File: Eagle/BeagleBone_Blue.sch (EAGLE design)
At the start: 146 parts, among them M1 JST_ZH_2, M2 JST_ZH_2, M3 JST_ZH_2, M4 JST_ZH_2, Q3 MOSFET-N, U1 OSD3358

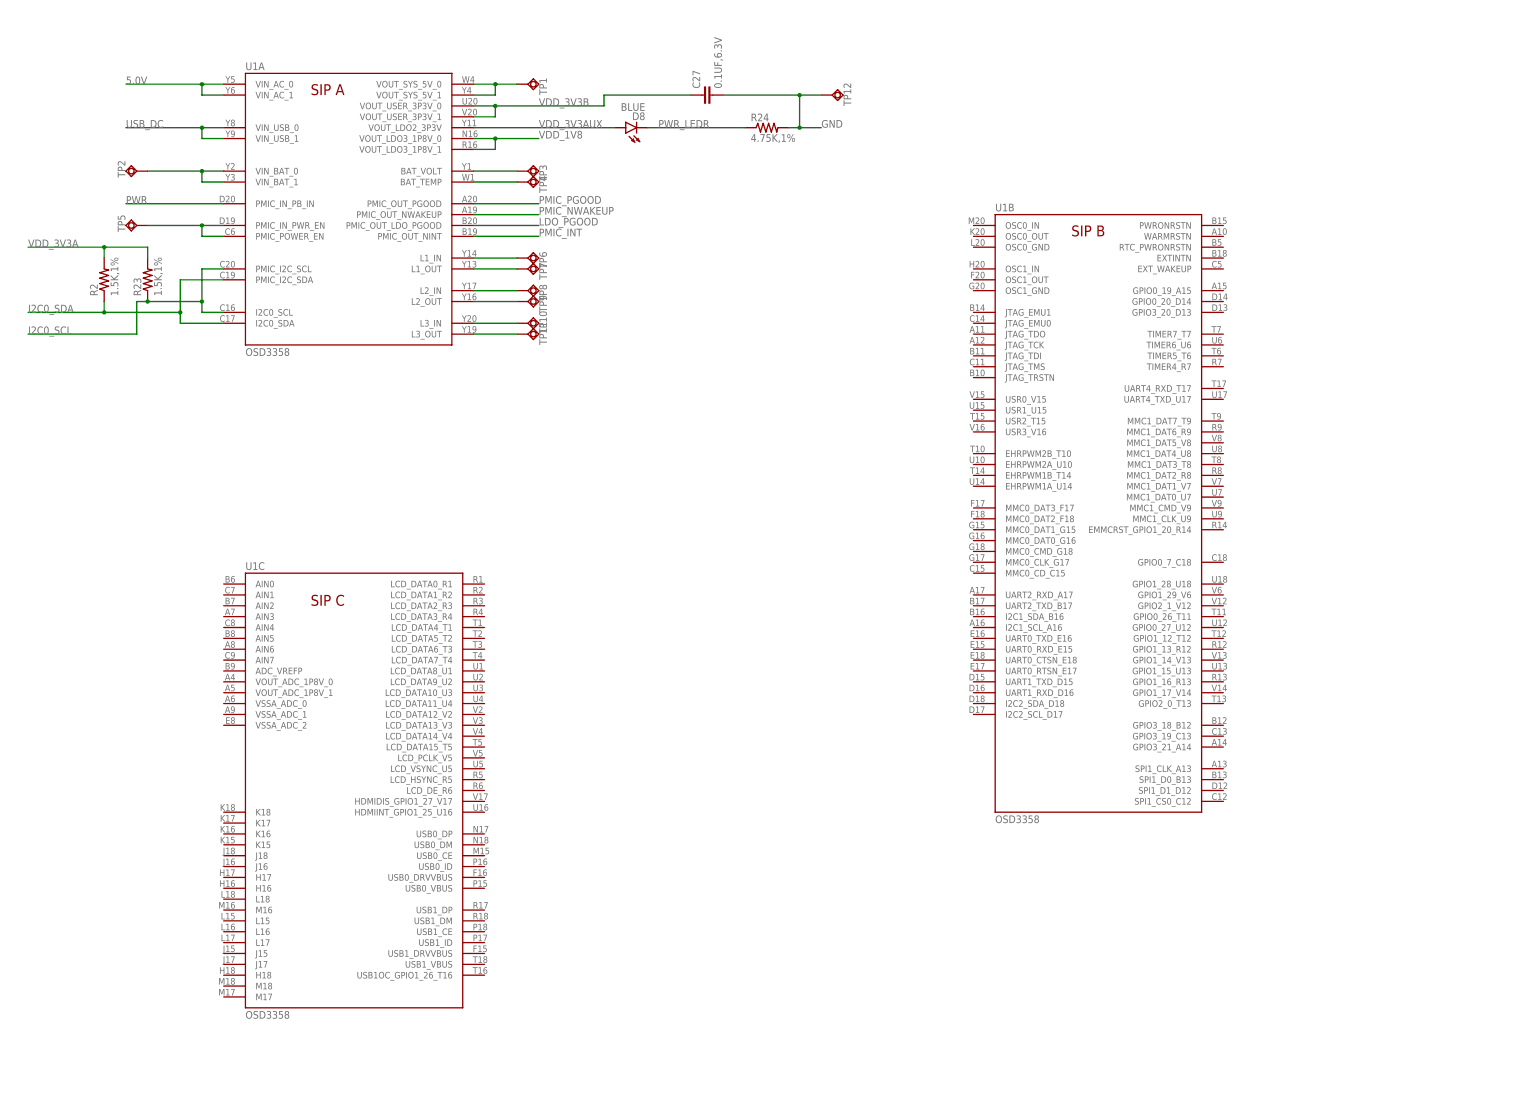
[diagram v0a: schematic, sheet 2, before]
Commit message: Add EEPROM
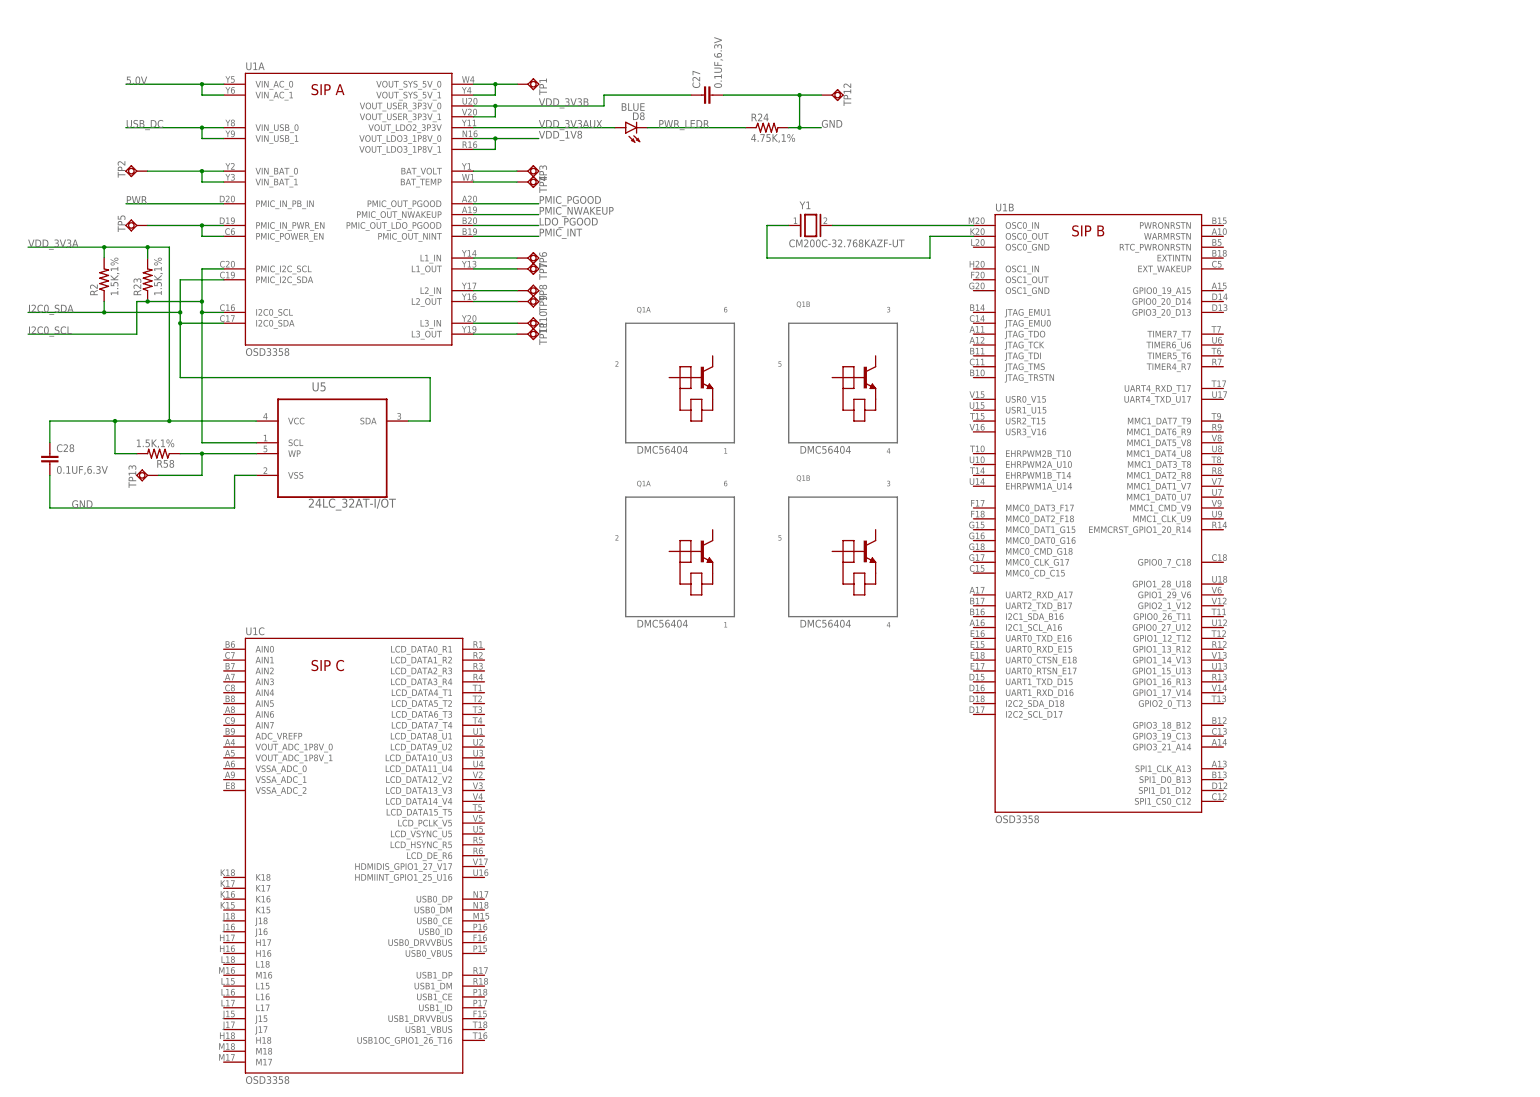
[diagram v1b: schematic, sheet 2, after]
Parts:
- added C28: 0.1UF,6.3V, Strawson_Eagle_Lib:CAP0402-CAP
- added R58: 1.5K,1%, Strawson_Eagle_Lib:RESISTOR0402-RES
- added TP13: TPSQB1,27, testpad:TPSQB1,27
- added U2: CM200C-32.768KAZF-UT, CM200C-32.768KAZF-UT:CM200C-32.768KAZF-UT
- added U3, U4: DMC564040R, DMC564040R:DMC564040R
- added U5: 24LC_32AT-I/OT, Microchip-24LCxxx:24LC_32AT-I/OT
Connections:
- new net N$26: U1B.OSC0_IN, U2.2
- new net N$27: U1B.OSC0_OUT, U2.1
- new net N$28: R58.1, TP13.TP, U5.WP
- net GND: now also C28.2, U5.VSS
- net I2C0_SDA: now also U5.SDA
- net VDD_3V3A: now also C28.1, R58.2, U5.VCC
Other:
- moved on the sheet: U1C
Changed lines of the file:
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@@
 <part name="TP12" library="testpad" deviceset="TPSQ" device="B1,27"/>
 <part name="C27" library="Strawson_Eagle_Lib" deviceset="CAP" device="0402-CAP" value="0.1UF,6.3V"/>
+<part name="U2" library="CM200C-32.768KAZF-UT" deviceset="CM200C-32.768KAZF-UT" device=""/>
+<part name="U3" library="DMC564040R" deviceset="DMC564040R" device=""/>
+<part name="U4" library="DMC564040R" deviceset="DMC564040R" device=""/>
+<part name="U5" library="Microchip-24LCxxx" deviceset="24LC_" device="" technology="32AT-I/OT"/>
+<part name="R58" library="Strawson_Eagle_Lib" deviceset="RESISTOR" device="0402-RES" value="1.5K,1%"/>
+<part name="TP13" library="testpad" deviceset="TPSQ" device="B1,27"/>
+<part name="C28" library="Strawson_Eagle_Lib" deviceset="CAP" device="0402-CAP" value="0.1UF,6.3V"/>
 </parts>
 <sheets>
@@
 <instance part="U1" gate="B" x="246.38" y="78.74"/>
 <instance part="U1" gate="A" x="71.12" y="187.96"/>
-<instance part="U1" gate="C" x="71.12" y="33.02"/>
+<instance part="U1" gate="C" x="71.12" y="17.78"/>
 <instance part="TP1" gate="G$1" x="137.16" y="248.92" rot="R90"/>
 <instance part="TP2" gate="G$1" x="45.72" y="228.6" rot="R270"/>
@@
 <instance part="TP12" gate="G$1" x="208.28" y="246.38" rot="R90"/>
 <instance part="C27" gate="G$1" x="180.34" y="246.38" rot="R90"/>
+<instance part="U2" gate="G$1" x="251.46" y="203.2"/>
+<instance part="U3" gate="G$1" x="195.58" y="175.26"/>
+<instance part="U4" gate="G$1" x="195.58" y="134.62"/>
+<instance part="U5" gate="A" x="73.66" y="170.18"/>
+<instance part="R58" gate="G$1" x="50.8" y="162.56" rot="R180"/>
+<instance part="TP13" gate="G$1" x="48.26" y="157.48" rot="R270"/>
+<instance part="C28" gate="G$1" x="25.4" y="160.02"/>
 </instances>
 <busses>
@@
 <wire x1="45.72" y1="190.5" x2="20.32" y2="190.5" width="0.1524" layer="91"/>
 <label x="20.32" y="190.5" size="1.778" layer="95"/>
+<wire x1="60.96" y1="195.58" x2="60.96" y2="165.1" width="0.1524" layer="91"/>
+<junction x="60.96" y="195.58"/>
+<wire x1="60.96" y1="165.1" x2="73.66" y2="165.1" width="0.1524" layer="91"/>
 </segment>
 </net>
@@
 <junction x="38.1" y="195.58"/>
 <label x="20.32" y="195.58" size="1.778" layer="95"/>
+<wire x1="55.88" y1="193.04" x2="55.88" y2="180.34" width="0.1524" layer="91"/>
+<junction x="55.88" y="193.04"/>
+<wire x1="55.88" y1="180.34" x2="114.3" y2="180.34" width="0.1524" layer="91"/>
+<wire x1="114.3" y1="180.34" x2="114.3" y2="170.18" width="0.1524" layer="91"/>
+<wire x1="114.3" y1="170.18" x2="109.22" y2="170.18" width="0.1524" layer="91"/>
+<pinref part="U5" gate="A" pin="SDA"/>
 </segment>
 </net>
@@
 <junction x="38.1" y="210.82"/>
 <label x="20.32" y="210.82" size="1.778" layer="95"/>
+<wire x1="48.26" y1="210.82" x2="53.34" y2="210.82" width="0.1524" layer="91"/>
+<junction x="48.26" y="210.82"/>
+<wire x1="53.34" y1="210.82" x2="53.34" y2="170.18" width="0.1524" layer="91"/>
+<pinref part="U5" gate="A" pin="VCC"/>
+<wire x1="53.34" y1="170.18" x2="73.66" y2="170.18" width="0.1524" layer="91"/>
+<wire x1="53.34" y1="170.18" x2="40.64" y2="170.18" width="0.1524" layer="91"/>
+<junction x="53.34" y="170.18"/>
+<wire x1="40.64" y1="170.18" x2="40.64" y2="162.56" width="0.1524" layer="91"/>
+<pinref part="R58" gate="G$1" pin="2"/>
+<wire x1="40.64" y1="162.56" x2="45.72" y2="162.56" width="0.1524" layer="91"/>
+<pinref part="C28" gate="G$1" pin="1"/>
+<wire x1="40.64" y1="170.18" x2="25.4" y2="170.18" width="0.1524" layer="91"/>
+<wire x1="25.4" y1="170.18" x2="25.4" y2="165.1" width="0.1524" layer="91"/>
+<junction x="40.64" y="170.18"/>
 </segment>
 </net>
@@
 <junction x="200.66" y="238.76"/>
 </segment>
+<segment>
+<pinref part="U5" gate="A" pin="VSS"/>
+<wire x1="73.66" y1="157.48" x2="68.58" y2="157.48" width="0.1524" layer="91"/>
+<wire x1="68.58" y1="157.48" x2="68.58" y2="149.86" width="0.1524" layer="91"/>
+<wire x1="68.58" y1="149.86" x2="25.4" y2="149.86" width="0.1524" layer="91"/>
+<pinref part="C28" gate="G$1" pin="2"/>
+<wire x1="25.4" y1="149.86" x2="25.4" y2="157.48" width="0.1524" layer="91"/>
+<label x="30.48" y="149.86" size="1.778" layer="95"/>
+</segment>
 </net>
 <net name="VDD_1V8" class="0">
@@
 </segment>
 </net>
+<net name="N$26" class="0">
+<segment>
+<pinref part="U1" gate="B" pin="OSC0_IN"/>
+<pinref part="U2" gate="G$1" pin="2"/>
+<wire x1="241.3" y1="215.9" x2="208.28" y2="215.9" width="0.1524" layer="91"/>
+</segment>
+</net>
+<net name="N$27" class="0">
+<segment>
+<pinref part="U1" gate="B" pin="OSC0_OUT"/>
+<wire x1="241.3" y1="213.36" x2="231.14" y2="213.36" width="0.1524" layer="91"/>
+<wire x1="231.14" y1="213.36" x2="231.14" y2="208.28" width="0.1524" layer="91"/>
+<wire x1="231.14" y1="208.28" x2="193.04" y2="208.28" width="0.1524" layer="91"/>
+<wire x1="193.04" y1="208.28" x2="193.04" y2="215.9" width="0.1524" layer="91"/>
+<pinref part="U2" gate="G$1" pin="1"/>
+<wire x1="193.04" y1="215.9" x2="198.12" y2="215.9" width="0.1524" layer="91"/>
+</segment>
+</net>
+<net name="N$28" class="0">
+<segment>
+<pinref part="R58" gate="G$1" pin="1"/>
+<pinref part="U5" gate="A" pin="WP"/>
+<wire x1="55.88" y1="162.56" x2="60.96" y2="162.56" width="0.1524" layer="91"/>
+<pinref part="TP13" gate="G$1" pin="TP"/>
+<wire x1="60.96" y1="162.56" x2="73.66" y2="162.56" width="0.1524" layer="91"/>
+<wire x1="50.8" y1="157.48" x2="60.96" y2="157.48" width="0.1524" layer="91"/>
+<wire x1="60.96" y1="157.48" x2="60.96" y2="162.56" width="0.1524" layer="91"/>
+<junction x="60.96" y="162.56"/>
+</segment>
+</net>
